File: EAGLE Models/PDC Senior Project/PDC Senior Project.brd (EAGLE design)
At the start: 160 x 100 mm, 158 parts, among them IC1 AT90CAN128, IC2 MCP2551SO8, IC3 NUP2105L, IC5 FT232RL, M1 PSMN2R2-25YLC, M11 PSMN2R2-25YLC, M12 PSMN2R2-25YLC, M2 PSMN2R2-25YLC, M3 PSMN2R2-25YLC, M4 PSMN2R2-25YLC, M5 PSMN2R2-25YLC, M6 PSMN2R2-25YLC, M7 PSMN2R2-25YLC, M8 PSMN2R2-25YLC, M9 PSMN2R2-25YLC, Q1 56P2859, U1 LT6100HMS8PBF, U10 LT6100HMS8PBF, U11 LT1161ISWPBF, U12 LT1161ISWPBF, U13 LT6100HMS8PBF, U14 LT6100HMS8PBF, U15 LT6100HMS8PBF, U16 LT6100HMS8PBF, U17 LT6100HMS8PBF, U18 LT6100HMS8PBF, U19 LT6100HMS8PBF, U2 LT1716IS5PBF, U20 DG409DY-E3, U21 AD5314WARMZ-REEL7, U22 LT1910IS8TRPBF, U3 LT1161ISWPBF, U4 LT1716IS5PBF, U5 LT1716IS5PBF, U6 LT1716IS5PBF, U7 LT6100HMS8PBF, U8 LT6100HMS8PBF, U9 LT6100HMS8PBF

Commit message: Routing Updates
Routed MUX and other signals. Started routing microcontroller.
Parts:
- moved U5 718.9 mm to (97.0, 27.1)
- moved U4 701.1 mm to (97.0, 30.2)
- moved U2 683.4 mm to (97.0, 33.5)
- moved U12 630.4 mm to (86.9, 15.5), turned to 180 degrees
- moved R47 625.5 mm to (42.2, 6.86), turned to 270 degrees
- moved R14 584.0 mm to (101.0, 17.3), turned to 270 degrees
- moved R16 583.8 mm to (98.9, 20.3), turned to 270 degrees
- moved R15 583.0 mm to (101.0, 20.3), turned to 90 degrees
- moved R13 581.5 mm to (98.9, 17.3), turned to 90 degrees
- moved U$21 581.3 mm to (48.5, 90.0), turned to 270 degrees
- moved U3 575.3 mm to (90.3, 43.9), turned to 180 degrees
- moved U11 573.7 mm to (87.1, 80.0), flipped to the bottom
- moved R12 559.6 mm to (98.8, 39.8), turned to 90 degrees
- moved R11 558.8 mm to (100.8, 39.8), turned to 270 degrees
- moved R5 557.3 mm to (98.8, 36.7), turned to 90 degrees
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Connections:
- removed net N$102: U$25.A27
- removed net N$103: U$25.A28
- net D+: now also U$25.A27
- net D-: now also U$25.A28
- net GND: now also H1.P$1, H2.P$1, H3.P$1, H4.P$1
- net HC1_ISENSE: now also U20.5; no longer U20.4
- net HC1_VSENSE: now also U20.12; no longer U20.13
- net HC2_ISENSE: now also U20.7; no longer U20.5
- net HC2_VSENSE: now also U20.10; no longer U20.12
- net HC4_ISENSE: now also U20.4; no longer U20.7
- net HC4_VSENSE: now also U20.13; no longer U20.10
- net PB5(PWM): now also U$3.14
- net PB6(PWM): now also U$3.12
- net PB7(PWM): now also U$3.10
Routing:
- net PC0: track 0.00 -> 168.4 mm, vias 0 -> 4
- net HC3_ISENSE: track 0.00 -> 166.3 mm, vias 0 -> 1
- net PA2: track 0.00 -> 151.2 mm, vias 0 -> 1
- net PA1: track 0.00 -> 151.2 mm, vias 0 -> 1
- net 12V: track 0.00 -> 145.5 mm, vias 0 -> 2
- net PC1: track 0.00 -> 145.1 mm, vias 0 -> 8
- net HC3_GATE: track 0.00 -> 142.6 mm, vias 0 -> 5
- net HC2_GATE: track 0.00 -> 130.6 mm, vias 0 -> 6
- net ADC1: track 0.00 -> 101.1 mm, vias 0 -> 3
- net ADC0: track 0.00 -> 98.0 mm, vias 0 -> 1
- net LC5_VSENSE: track 0.00 -> 97.8 mm, vias 0 -> 1
- net HC4_ISENSE: track 0.00 -> 94.1 mm, vias 0 -> 3
- net HC1_GATE: track 0.00 -> 92.6 mm, vias 0 -> 3
- net HC1_ISENSE: track 0.00 -> 90.5 mm, vias 0 -> 3
- net LC6_VSENSE: track 0.00 -> 87.5 mm, vias 0 -> 1
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
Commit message: fixed some DRC errors and added ground planes
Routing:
- net PC0: track 168.4 -> 168.2 mm, vias 4 -> 6
- added copper zone on layer 1, net GND
- added copper zone on layer 16, net GND

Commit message: Signal Routing
Routed FTDI, CAN transiever, reset, current sense, input limiter, and
oscillator. Changed pinout on connector to aid routing
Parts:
- moved C10 686.8 mm to (64.4, 64.1), flipped to the bottom, turned to 270 degrees
- moved C8 681.3 mm to (41.0, 37.8), flipped to the bottom, turned to 90 degrees
- moved C6 666.2 mm to (46.2, 54.1), flipped to the bottom, turned to 270 degrees
- moved C7 660.4 mm to (32.5, 53.8), flipped to the bottom, turned to 270 degrees
- moved C5 659.9 mm to (26.8, 39.8), flipped to the bottom, turned to 270 degrees
- moved LED3 589.5 mm to (10.8, 88.0), turned to 270 degrees
- moved LED2 583.9 mm to (10.8, 89.9), turned to 270 degrees
- moved U$24 562.9 mm to (3.43, 71.5), flipped to the bottom
- moved U$22 562.5 mm to (2.79, 54.7), flipped to the bottom, turned to 180 degrees
- moved U$23 560.9 mm to (3.43, 65.2), flipped to the bottom
- moved R45 554.6 mm to (3.05, 61.5), flipped to the bottom, turned to 270 degrees
- moved R41 552.0 mm to (6.22, 57.7), flipped to the bottom, turned to 180 degrees
- moved R42 551.6 mm to (6.35, 60.3), flipped to the bottom, turned to 180 degrees
- moved R46 551.5 mm to (6.48, 69.3), flipped to the bottom, turned to 180 degrees
- moved R43 550.9 mm to (6.60, 63.4), flipped to the bottom, turned to 180 degrees
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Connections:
- net CAN_H: now also U$25.A29; no longer U$25.A25
- net CAN_L: now also U$25.A30; no longer U$25.A34
- net GND: now also U$25.A25, U$25.A34; no longer U$25.A22, U$25.A23
- net INPUT1: now also U$25.A14; no longer U$25.A5
- net INPUT2: now also U$25.A23; no longer U$25.B4
- net INPUT3: now also U$25.A31; no longer U$25.A6
- net INPUT4: now also U$25.A22; no longer U$25.A14
- net INPUT_PIN_5: now also U$24.1; no longer U$24.2
- net INPUT_PIN_6: now also U$24.2; no longer U$24.1
- net N$104: now also U$25.A5; no longer U$25.A29
- net N$105: now also U$25.A6; no longer U$25.A30
- net N$106: now also U$25.B4; no longer U$25.A31
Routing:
- net PA4: track 0.00 -> 190.7 mm, vias 0 -> 1
- net PA3: track 0.00 -> 183.1 mm, vias 0 -> 1
- net AVR_SCK: track 0.00 -> 152.7 mm, vias 0 -> 3
- net AVR_MOSI: track 0.00 -> 152.7 mm, vias 0 -> 3
- net AVR_CS: track 0.00 -> 151.4 mm, vias 0 -> 3
- net PB4(PWM): track 0.00 -> 139.2 mm, vias 0 -> 2
- net PB5(PWM): track 0.00 -> 138.6 mm, vias 0 -> 2
- net PB6(PWM): track 0.00 -> 138.4 mm, vias 0 -> 2
- net PB7(PWM): track 0.00 -> 133.2 mm, vias 0 -> 2
- net PE5(PWM): track 0.00 -> 72.7 mm, vias 0 -> 2
- net PE4(PWM): track 0.00 -> 67.3 mm, vias 0 -> 2
- net PE3(PWM): track 0.00 -> 62.0 mm, vias 0 -> 2
- net M8TXD: track 0.00 -> 38.5 mm, vias 0 -> 2
- net INPUT_PIN_5: track 33.4 -> 1.96 mm, vias 2 -> 0
- net CAN_L: track 0.00 -> 31.4 mm, vias 0 -> 1
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
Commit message: added VCC and signal routing
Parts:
- removed C15: 10uF, resistor:C2220
- removed C3, C4: 22uF, resistor:C2220
- removed L2: 22uH, inductors:DR73
- removed U$1: V7805-1000, formula electric:V78XX-1000
- added C23, C24: (no value), rcl:C0603
- added U$26: NCP1117, on-semiconductor:SOT-223-4
- moved VCC! 674.3 mm to (99.8, 85.6), turned to 180 degrees
- moved D2 650.3 mm to (97.3, 75.6), turned to 270 degrees
- moved H4 561.3 mm to (3.56, 101.6)
- moved R10 558.3 mm to (105.7, 40.8), turned to 90 degrees
- moved H7 527.9 mm to (29.6, 94.4)
- moved R6 484.8 mm to (98.6, 88.8), turned to 180 degrees
- moved F1 482.1 mm to (20.1, 64.9), flipped to the bottom, turned to 90 degrees
- moved D1 6.63 mm to (32.8, 87.6), turned to 180 degrees
- moved SJ1 4.04 mm to (29.2, 86.1), turned to 90 degrees
- moved R1 2.72 mm to (34.4, 90.0)
- moved C16 2.71 mm to (31.8, 86.4)
- moved C19 0.38 mm to (26.0, 83.9)
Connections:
- removed net 12V_PROTECTED: C15.1, D2.C, U$1.1
- removed net N$101 (its old number): U$25.A4
- removed net N$13: C3.1, L2.1, U$1.5
- new net 5V_REG_IN: C23.1, D2.C, U$26.3
- net ANALOG_EMERGENCY_SHUTDOWN: now also U$25.A4
- net GND: now also C23.2, C24.2, U$26.1; no longer C15.2, C3.2, C4.2, U$1.7, U$1.9
- net VCC: now also C24.1, U$26.2, U$26.4; no longer C4.1, L2.2
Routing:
- net VCC: track 28.7 -> 451.7 mm, vias 1 -> 27
- net ANALOG_EMERGENCY_SHUTDOWN: track 0.00 -> 207.8 mm, vias 0 -> 5
- net INPUT_PIN_1: track 3.10 -> 91.1 mm, vias 0 -> 2
- net INPUT_PIN_2: track 7.07 -> 86.6 mm, vias 0 -> 2
- net INPUT_PIN_6: track 6.01 -> 84.8 mm, vias 0 -> 2
- net INPUT_PIN_5: track 1.96 -> 78.0 mm, vias 0 -> 2
- net INPUT_PIN_4: track 1.66 -> 65.8 mm, vias 0 -> 2
- net INPUT_PIN_3: track 1.97 -> 63.5 mm, vias 0 -> 4
- net 12V: track 145.5 -> 187.5 mm, vias 2 -> 8
- net TX: track 2.96 -> 30.2 mm, vias 0 -> 3
- net RX: track 2.88 -> 29.6 mm, vias 0 -> 3
- net AVR_SCK: track 152.7 -> 169.9 mm, vias 3 -> 6
- net RESET: track 8.79 -> 19.3 mm, vias 0 -> 1
- net 5V_REG_IN: track 0.00 -> 6.71 mm
- net M8RXD: track 28.1 -> 33.5 mm
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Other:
- board size 160 x 100 mm -> 160 x 106.7 mm

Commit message: Ground Routing, Signal Routing, and DRC fixes
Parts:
- moved H2 721.3 mm to (152.1, 6.16)
- moved C9 679.7 mm to (57.2, 61.4), flipped to the bottom, turned to 270 degrees
- moved H1 649.7 mm to (150.9, 99.8)
- moved H3 635.1 mm to (3.62, 3.62)
- moved L1 555.8 mm to (48.4, 85.1), turned to 180 degrees
- moved C12 500.8 mm to (21.5, 58.3)
- moved C14 5.78 mm to (55.7, 31.3)
- moved R36 1.91 mm to (30.1, 74.5), turned to 90 degrees
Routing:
- net VCC: track 451.7 -> 517.7 mm, vias 27 -> 31
- net HC3_DISCH_TRIGGER: track 5.16 -> 35.6 mm, vias 0 -> 2
- net HC2_DISCH_TRIGGER: track 5.36 -> 23.4 mm
- net HC4_ANALOG_BACKUP_REF: track 0.00 -> 14.5 mm, vias 0 -> 2
- net N$7: track 2.03 -> 14.7 mm, vias 0 -> 2
- net PA3: track 183.1 -> 192.5 mm, vias 1 -> 3
- net RESET: track 19.3 -> 28.7 mm
- net HC4_DISCH_TRIGGER: track 5.41 -> 14.1 mm
- net N$53: track 4.45 -> 9.90 mm
- net N$31: track 0.00 -> 5.17 mm
- net HC1_DISCH_TRIGGER: track 5.90 -> 10.6 mm
- net N$14: track 20.5 -> 25.1 mm
- net N$22: track 0.00 -> 4.07 mm, vias 0 -> 1
- net N$28: track 6.84 -> 4.67 mm
- net LC4_OUTPUT: track 96.5 -> 95.2 mm
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
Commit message: completed routing
completed all routing
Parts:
- moved C18 1.59 mm to (23.8, 78.4)
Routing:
- net HC3_DISCH_TRIGGER: track 35.6 -> 41.2 mm
- net HC4_DISCH_TRIGGER: track 14.1 -> 18.5 mm
- net N$35: track 0.00 -> 2.28 mm
- net VCC3O: track 7.37 -> 8.90 mm
- net HC2_DISCH_TRIGGER: track 23.4 -> 22.3 mm
- net VCC: track 517.7 -> 518.0 mm, vias 31 -> 32
- net GND: vias 53 -> 67

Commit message: Added 5V reference for ADC
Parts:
- moved H1 43.5 mm to (107.4, 99.3)
- moved H2 42.7 mm to (109.3, 5.84)
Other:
- outline, holes or cut-outs redrawn
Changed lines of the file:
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@@
 <wire x1="160" y1="0" x2="160" y2="106.68" width="0" layer="20"/>
 <wire x1="160" y1="106.68" x2="0" y2="106.68" width="0" layer="20"/>
-<wire x1="0" y1="106.68" x2="0" y2="0" width="0" layer="20"/>
+<wire x1="0" y1="106.68" x2="0" y2="103.124" width="0" layer="20"/>
+<wire x1="0" y1="98.2345" x2="0" y2="0" width="0" layer="20"/>
+<wire x1="0" y1="98.2345" x2="0" y2="103.124" width="0" layer="20"/>
 </plain>
 <attributes>
@@
 <attribute name="OC_NEWARK" value="18M4796" x="76.2" y="41.91" size="1.778" layer="27" rot="R270" display="off"/>
 </element>
-<element name="H1" library="holes" package="#4-40-PAD-ROUND" value="MOUNT-PAD-ROUND#4-40-PAD" x="150.876" y="99.822"/>
-<element name="H2" library="holes" package="#4-40-PAD-ROUND" value="MOUNT-PAD-ROUND#4-40-PAD" x="152.0825" y="6.1595"/>
+<element name="H1" library="holes" package="#4-40-PAD-ROUND" value="MOUNT-PAD-ROUND#4-40-PAD" x="107.3785" y="99.314"/>
+<element name="H2" library="holes" package="#4-40-PAD-ROUND" value="MOUNT-PAD-ROUND#4-40-PAD" x="109.347" y="5.842"/>
 <element name="H3" library="holes" package="#4-40-PAD-ROUND" value="MOUNT-PAD-ROUND#4-40-PAD" x="3.6195" y="3.6195"/>
 <element name="H4" library="holes" package="#4-40-PAD-ROUND" value="MOUNT-PAD-ROUND#4-40-PAD" x="3.556" y="101.6"/>

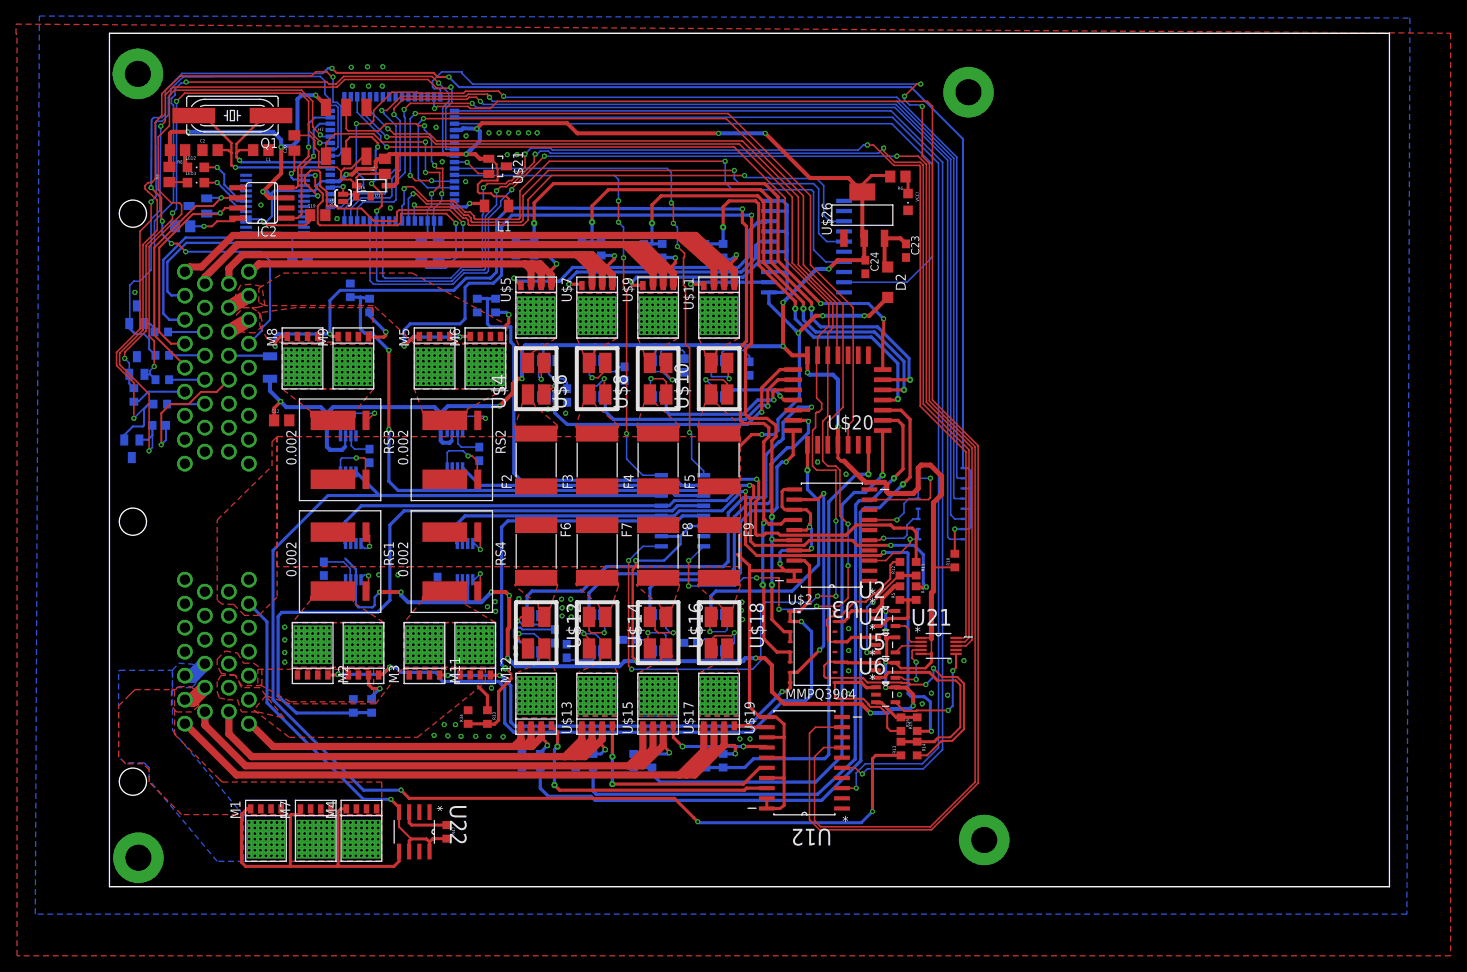
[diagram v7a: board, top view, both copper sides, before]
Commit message: Redimention Board, Fix Silkscreen
Made board outline smaller. Rounded corners to fit milled enclosure.
Dimentioned the board outline to ensure proper distance from connector
to board edge. Cleaned up silkscreen layers
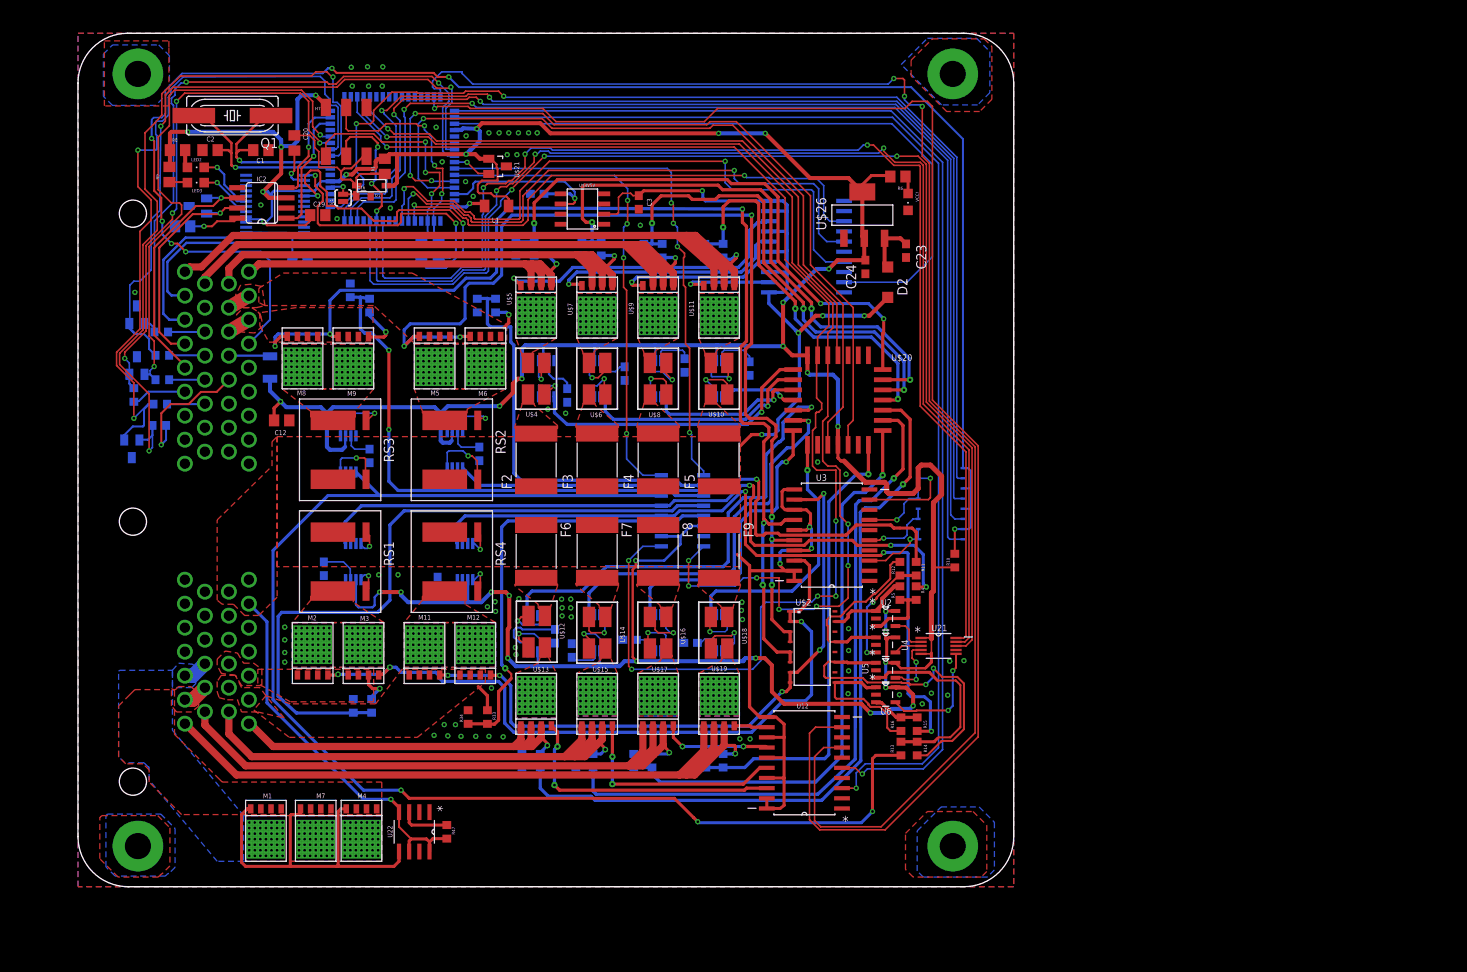
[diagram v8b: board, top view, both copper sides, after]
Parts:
- added C3, C4: 2.2uF, rcl:C0603
- added U$4V5V: MAX6350CSA, DashAndCAN library:8-SOIC
- moved H2 4.01 mm to (105.4, 5.08)
- moved H1 3.02 mm to (105.4, 101.6)
- moved H3 1.46 mm to (3.56, 5.08)
- moved C17 0.64 mm to (57.8, 29.5)
- moved U$12 0.14 mm to (53.4, 31.9)
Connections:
- removed net AREF: IC1.62
- new net 5VREF: C4.1, IC1.62, U$4V5V.P6
- net 12V: now also C3.1, U$4V5V.P2
- net GND: now also C3.2, C4.2, U$4V5V.P4
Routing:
- net 12V: track 187.5 -> 211.7 mm, vias 8 -> 9
- net 5VREF: track 0.00 -> 23.8 mm, vias 0 -> 1
- net PA3: track 192.5 -> 186.6 mm
- net LC2_VSENSE: track 67.9 -> 71.9 mm
- net VCC: track 518.0 -> 514.8 mm
- net INPUT_PIN_2: track 86.1 -> 88.8 mm
- net PA4: track 190.7 -> 188.7 mm
- net N$58: track 4.83 -> 4.12 mm
- net GND: vias 67 -> 69
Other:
- board size 160 x 106.7 mm -> 117 x 106.7 mm
